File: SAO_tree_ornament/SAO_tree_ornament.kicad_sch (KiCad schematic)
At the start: 23 parts, among them J1 USB_C_Receptacle_USB2.0_16P, J2 Conn_02x03_Odd_Even, J3 Conn_01x02, J4 Conn_01x02, J5 Conn_QWIIC_Vertical, J6 Conn_ARM_SWD_TagConnect_TC203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, U1 HUSB238, U2 LMR51430, U4 MSPM0C110xSDSG

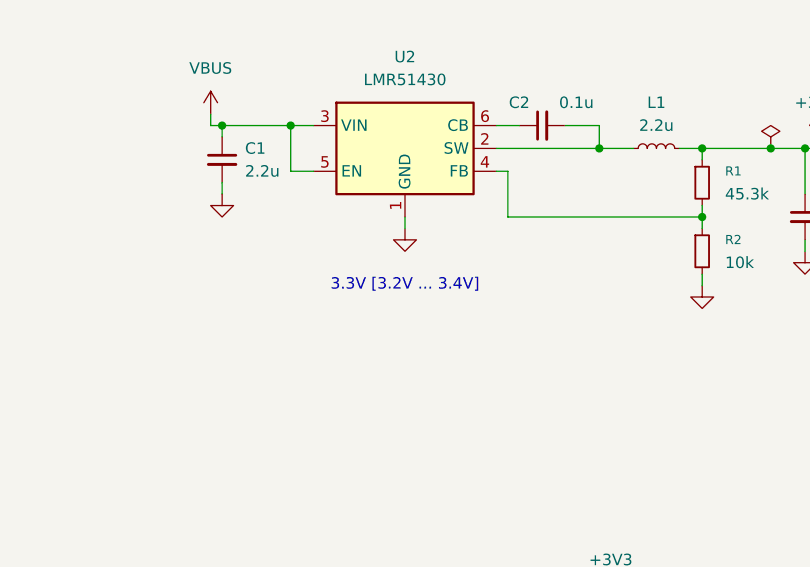
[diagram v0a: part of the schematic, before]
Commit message: Update SAO Connector on badge
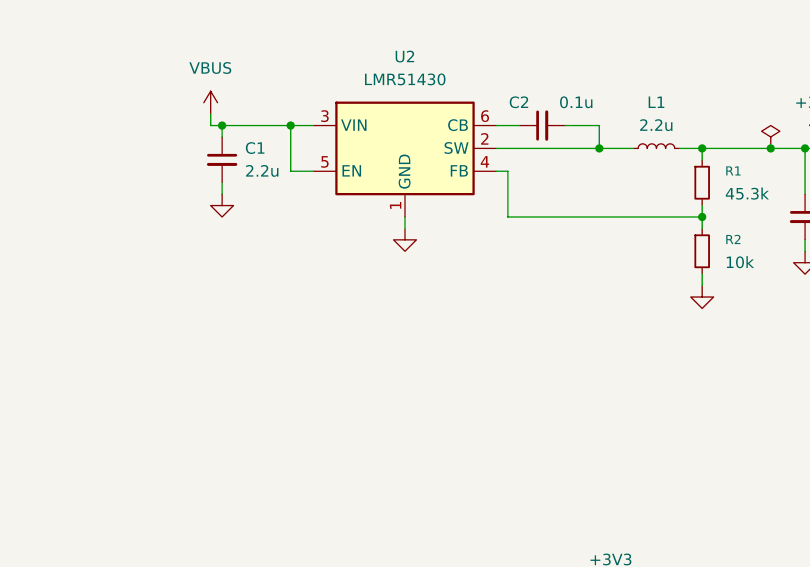
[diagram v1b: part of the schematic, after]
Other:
- note removed: "3.3V [3.2V ... 3.4V]"
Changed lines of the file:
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@@
-		)
-	)
-	(text "3.3V [3.2V ... 3.4V]"
-		(exclude_from_sim no)
-		(at 222.25 46.99 0)
-		(effects
-			(font
-				(size 1.27 1.27)
-			)
 		)
 	)

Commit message: Add finding of boot loop
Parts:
- J2: footprint Connector_PinSocket_2.54mm:PinSocket_2x03_P2.54mm_Vertical -> SKEC_Footprints:SAO_Connector_Badge
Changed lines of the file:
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@@
 			)
 		)
-		(property "Footprint" "Connector_PinSocket_2.54mm:PinSocket_2x03_P2.54mm_Vertical"
+		(property "Footprint" "SKEC_Footprints:SAO_Connector_Badge"
 			(at 237.49 87.63 0)
 			(effects
